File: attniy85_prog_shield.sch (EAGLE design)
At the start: 2 parts, among them U1 ARDUINOR3-BPLACE

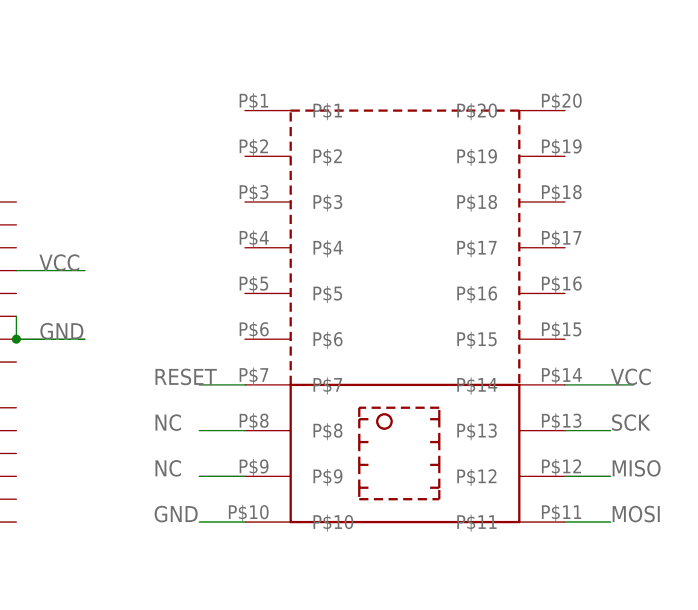
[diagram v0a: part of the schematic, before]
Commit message: correct zif width
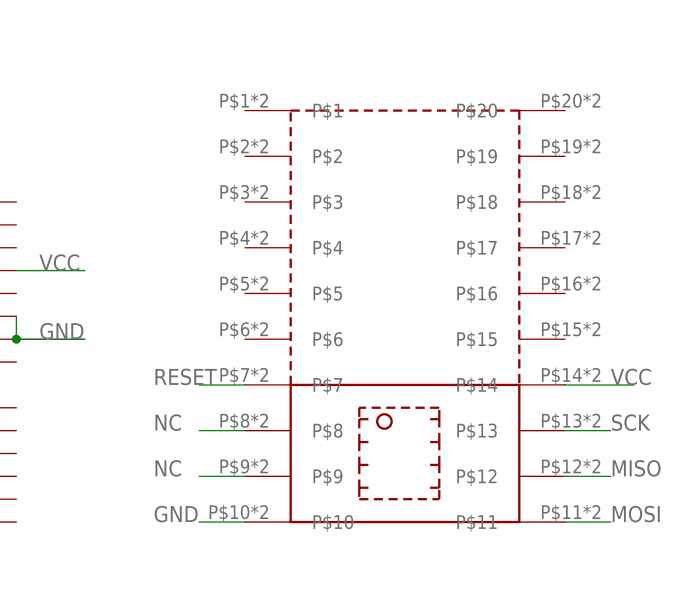
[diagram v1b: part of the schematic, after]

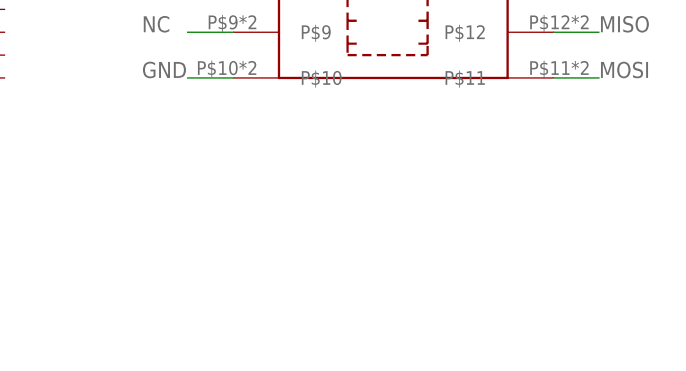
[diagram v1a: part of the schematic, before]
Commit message: unrouted 2x5pin isp
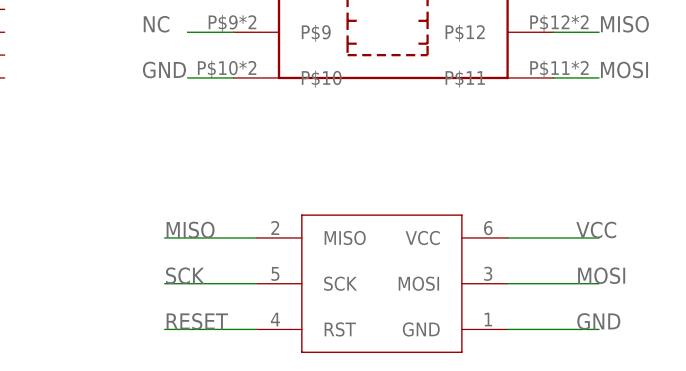
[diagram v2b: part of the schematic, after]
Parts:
- added X1: ISP10P, attniy85_prog_shield:ISP10P
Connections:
- net GND: now also X1.GND
- net MISO: now also X1.MISO
- net MOSI: now also X1.MOSI
- net RESET: now also X1.RST
- net SCK: now also X1.SCK
- net VCC: now also X1.VCC
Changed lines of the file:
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@@
 <part name="U1" library="ATtami" deviceset="ARDUINOR3" device="-BPLACE" value="ARDUINOR3-BPLACE"/>
 <part name="U$1" library="attniy85_prog_shield" deviceset="SOIC8_200MIL_PROG" device=""/>
+<part name="X1" library="attniy85_prog_shield" deviceset="ISP" device="10P"/>
 </parts>
 <sheets>
@@
 <instance part="U1" gate="G$1" x="-259.08" y="111.76" rot="MR270"/>
 <instance part="U$1" gate="G$1" x="-195.58" y="114.3"/>
+<instance part="X1" gate="G$1" x="-193.04" y="58.42"/>
 </instances>
 <busses>
@@
 <wire x1="-228.6" y1="116.84" x2="-220.98" y2="116.84" width="0.1524" layer="91"/>
 <label x="-226.06" y="116.84" size="1.778" layer="95"/>
+</segment>
+<segment>
+<pinref part="X1" gate="G$1" pin="VCC"/>
+<wire x1="-172.72" y1="71.12" x2="-162.56" y2="71.12" width="0.1524" layer="91"/>
+<label x="-165.1" y="71.12" size="1.778" layer="95"/>
 </segment>
 </net>
@@
 <label x="-213.36" y="88.9" size="1.778" layer="95"/>
 </segment>
+<segment>
+<pinref part="X1" gate="G$1" pin="GND"/>
+<wire x1="-172.72" y1="60.96" x2="-162.56" y2="60.96" width="0.1524" layer="91"/>
+<label x="-165.1" y="60.96" size="1.778" layer="95"/>
+</segment>
 </net>
 <net name="SCK" class="0">
@@
 <wire x1="-167.64" y1="99.06" x2="-162.56" y2="99.06" width="0.1524" layer="91"/>
 <label x="-162.56" y="99.06" size="1.778" layer="95"/>
+</segment>
+<segment>
+<pinref part="X1" gate="G$1" pin="SCK"/>
+<wire x1="-200.66" y1="66.04" x2="-210.82" y2="66.04" width="0.1524" layer="91"/>
+<label x="-210.82" y="66.04" size="1.778" layer="95"/>
 </segment>
 </net>
@@
 <label x="-162.56" y="93.98" size="1.778" layer="95"/>
 </segment>
+<segment>
+<pinref part="X1" gate="G$1" pin="MISO"/>
+<wire x1="-200.66" y1="71.12" x2="-210.82" y2="71.12" width="0.1524" layer="91"/>
+<label x="-210.82" y="71.12" size="1.778" layer="95"/>
+</segment>
 </net>
 <net name="MOSI" class="0">
@@
 <wire x1="-167.64" y1="88.9" x2="-162.56" y2="88.9" width="0.1524" layer="91"/>
 <label x="-162.56" y="88.9" size="1.778" layer="95"/>
+</segment>
+<segment>
+<pinref part="X1" gate="G$1" pin="MOSI"/>
+<wire x1="-172.72" y1="66.04" x2="-162.56" y2="66.04" width="0.1524" layer="91"/>
+<label x="-165.1" y="66.04" size="1.778" layer="95"/>
 </segment>
 </net>
@@
 <label x="-213.36" y="104.14" size="1.778" layer="95"/>
 </segment>
+<segment>
+<pinref part="X1" gate="G$1" pin="RST"/>
+<wire x1="-200.66" y1="60.96" x2="-210.82" y2="60.96" width="0.1524" layer="91"/>
+<label x="-210.82" y="60.96" size="1.778" layer="95"/>
+</segment>
 </net>
